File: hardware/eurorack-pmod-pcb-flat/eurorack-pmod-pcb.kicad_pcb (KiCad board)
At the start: 2 copper layers, 20 x 110 mm, 78 parts, among them J1 PMOD, J10 PJ398SM, J2 EURORACK_PWR, J3 PJ398SM, J4 PJ398SM, J5 PJ398SM, J6 PJ398SM, J7 PJ398SM, J8 PJ398SM, J9 PJ398SM, U1 LM1117-3.3, U2 TL072, U3 AK4619VN, U4 TL074, U5 TL074, U6 TL074, U7 TL074

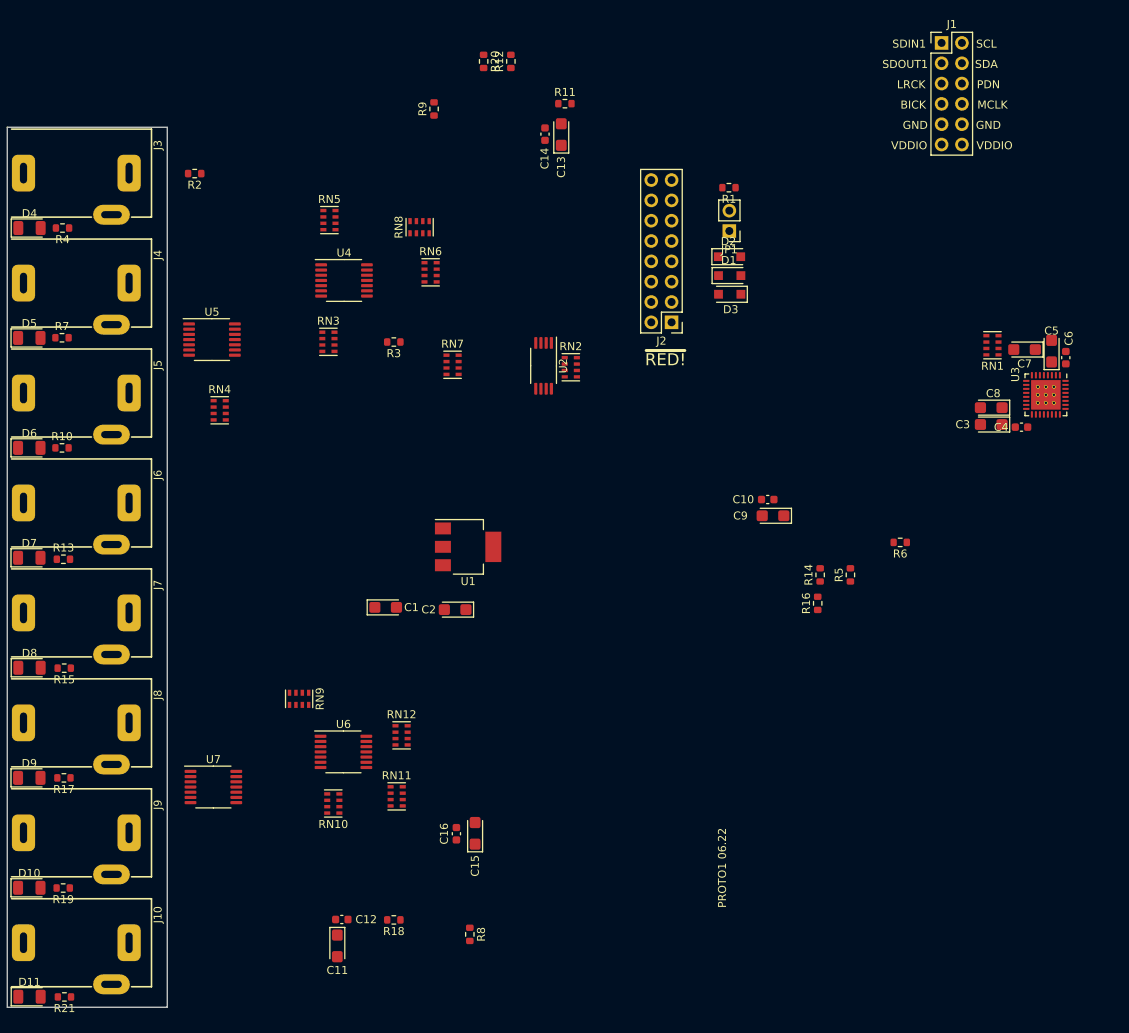
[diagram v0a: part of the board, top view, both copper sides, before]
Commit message: rev2-flat: add vref and stabilization caps
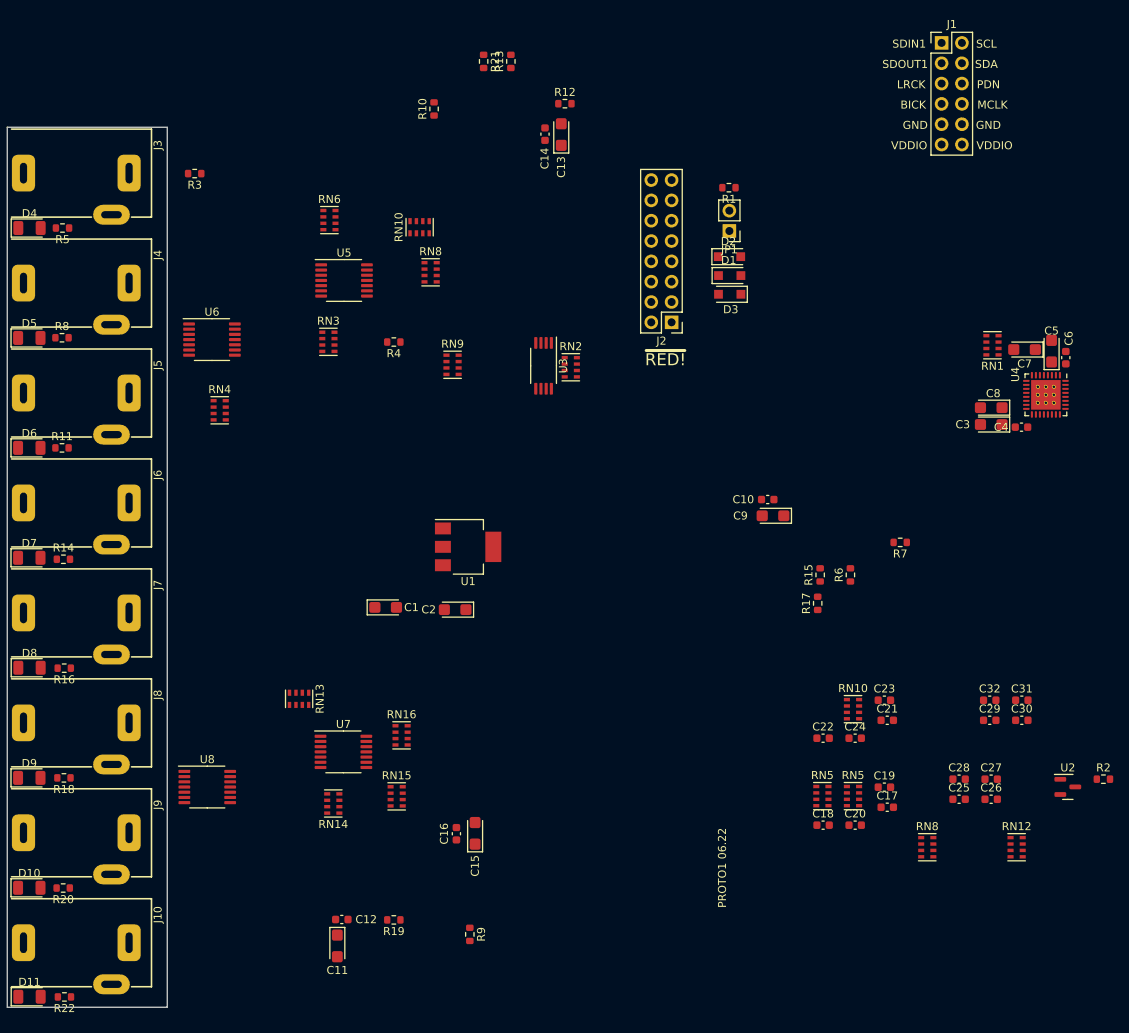
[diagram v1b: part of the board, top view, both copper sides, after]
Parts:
- added C17: 220p, Capacitor_SMD:C_0603_1608Metric, F.Cu at (90.0, 85.0)
- added C18: 220p, Capacitor_SMD:C_0603_1608Metric, F.Cu at (82.0, 87.2)
- added C19: 220p, Capacitor_SMD:C_0603_1608Metric, F.Cu at (89.6, 82.5)
- added C20: 220p, Capacitor_SMD:C_0603_1608Metric, F.Cu at (86.0, 87.2)
- added C21: 220p, Capacitor_SMD:C_0603_1608Metric, F.Cu at (90.0, 74.1)
- added C22: 220p, Capacitor_SMD:C_0603_1608Metric, F.Cu at (82.0, 76.4)
- added C23: 220p, Capacitor_SMD:C_0603_1608Metric, F.Cu at (89.6, 71.6)
- added C24: 220p, Capacitor_SMD:C_0603_1608Metric, F.Cu at (86.0, 76.4)
- added C25: 56p, Capacitor_SMD:C_0603_1608Metric, F.Cu at (99.0, 84.0)
- added C26: 220p, Capacitor_SMD:C_0603_1608Metric, F.Cu at (103.0, 84.0)
- added C27: 56p, Capacitor_SMD:C_0603_1608Metric, F.Cu at (103.0, 81.5)
- added C28: 220p, Capacitor_SMD:C_0603_1608Metric, F.Cu at (99.0, 81.5)
- added C29: 56p, Capacitor_SMD:C_0603_1608Metric, F.Cu at (102.8, 74.1)
- added C30: 220p, Capacitor_SMD:C_0603_1608Metric, F.Cu at (106.8, 74.1)
- added C31: 56p, Capacitor_SMD:C_0603_1608Metric, F.Cu at (106.8, 71.6)
- added C32: 220p, Capacitor_SMD:C_0603_1608Metric, F.Cu at (102.8, 71.6)
- added R2: 330R, Resistor_SMD:R_0603_1608Metric, F.Cu at (117.0, 81.5)
- added RN10: 15K, Resistor_SMD:R_Cat16-4, F.Cu at (85.7, 72.7)
- added RN12: 15K, Resistor_SMD:R_Cat16-4, F.Cu at (106.2, 90.0)
- added RN5: 15K, Resistor_SMD:R_Cat16-4, F.Cu at (85.7, 83.6)
- added RN5: 15K, Resistor_SMD:R_Cat16-4, F.Cu at (81.9, 83.6)
- added RN8: 15K, Resistor_SMD:R_Cat16-4, F.Cu at (95.0, 90.0)
- added U2: LM4040DBZ-3, Package_TO_SOT_SMD:SOT-23, F.Cu at (112.6, 82.5)
- moved U8 0.77 mm to (5.00, 82.5)
- renumbered R9 to R10, R10 to R11, R11 to R12, R12 to R13, R13 to R14, R14 to R15, R15 to R16, R16 to R17, R17 to R18, R18 to R19, R19 to R20, R20 to R21, R21 to R22, R2 to R3, R3 to R4, R4 to R5, R5 to R6, R6 to R7, R7 to R8, R8 to R9, RN8 to RN10, RN9 to RN13, RN10 to RN14, RN11 to RN15, RN12 to RN16, RN5 to RN6, RN6 to RN8, RN7 to RN9, U2 to U3, U3 to U4, U4 to U5, U5 to U6, U6 to U7, U7 to U8
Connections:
- J10 pad TN: GND -> unconnected-(J10-PadTN)
- J7 pad TN: GND -> unconnected-(J7-PadTN)
- J8 pad TN: GND -> unconnected-(J8-PadTN)
- J9 pad TN: GND -> unconnected-(J9-PadTN)
- RN2 pad 8: +3.3VA -> /VREFH
- U4 pad 21: +3.3VA -> /VREFH
- U6 pad 13: Net-(D7-Pad1) -> Net-(C24-Pad1)
- U6 pad 2: Net-(D4-Pad1) -> Net-(C18-Pad1)
- U6 pad 6: Net-(D5-Pad1) -> Net-(C20-Pad1)
- U6 pad 9: Net-(D6-Pad1) -> Net-(C22-Pad1)
- U8 pad 13: Net-(D11-Pad2) -> Net-(C32-Pad1)
- U8 pad 2: Net-(D8-Pad2) -> Net-(C26-Pad1)
- U8 pad 6: Net-(D9-Pad2) -> Net-(C28-Pad1)
- U8 pad 9: Net-(D10-Pad2) -> Net-(C30-Pad1)

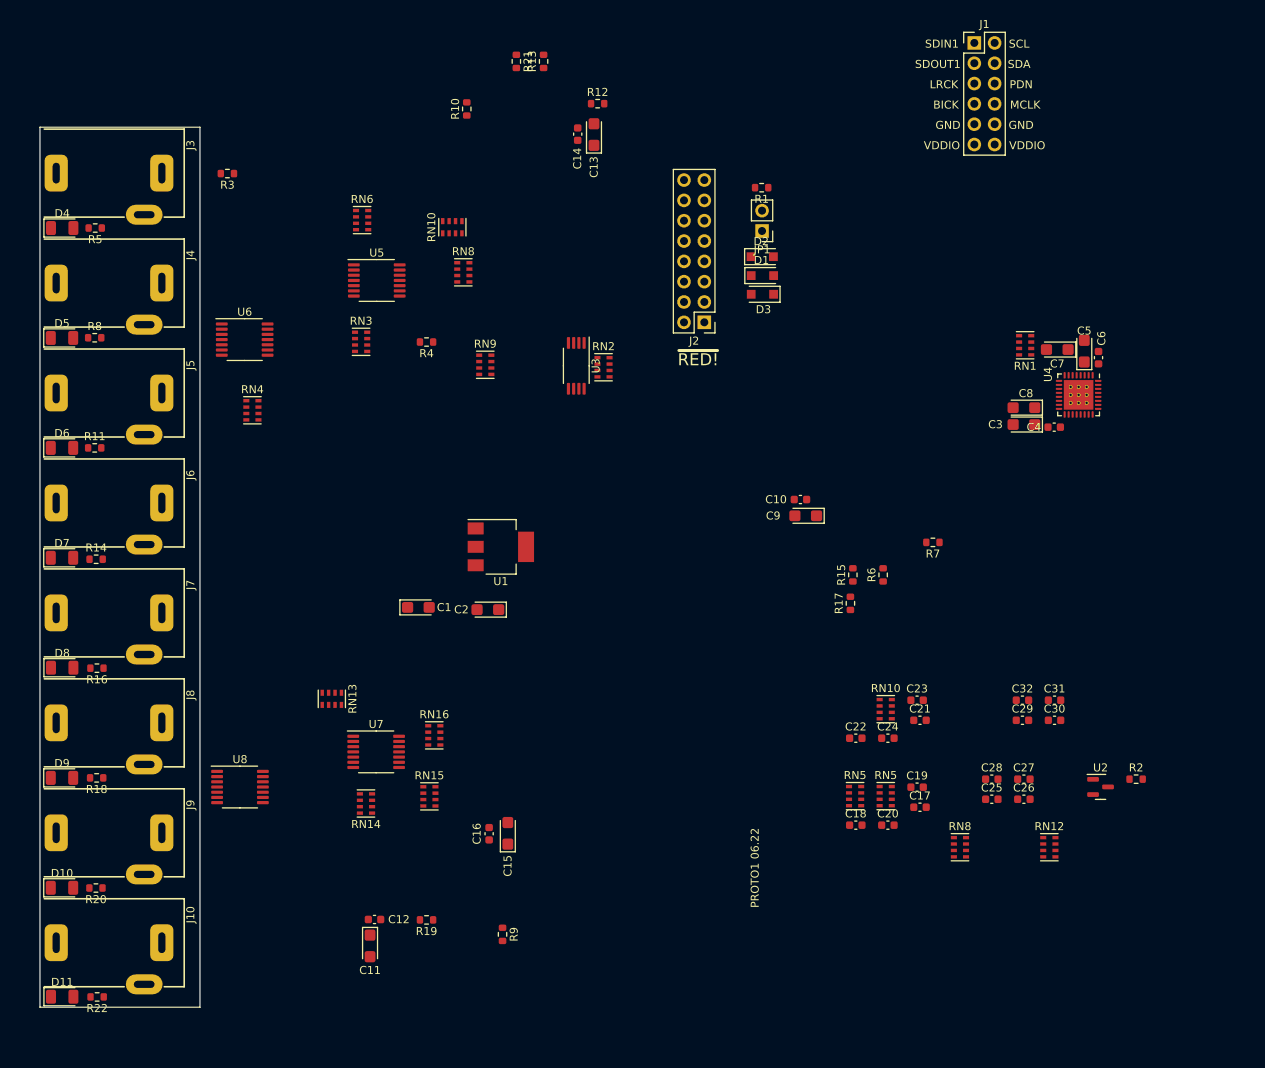
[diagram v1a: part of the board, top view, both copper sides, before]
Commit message: rev2-flat: update power supply and add bypass electros
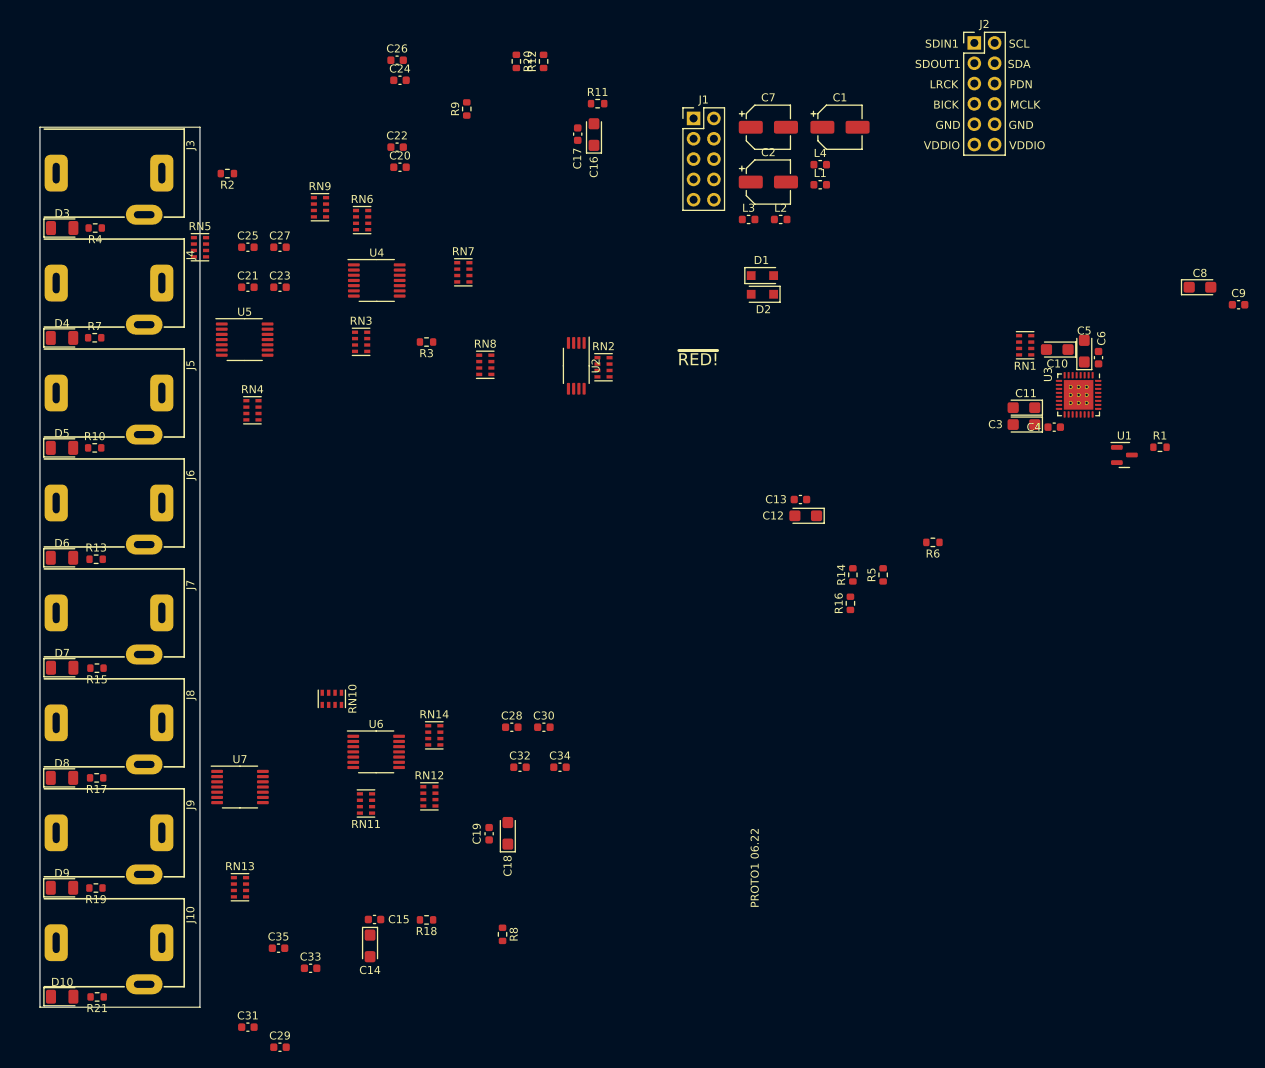
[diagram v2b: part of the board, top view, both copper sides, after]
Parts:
- removed the D2 at (70.3, 16.2)
- removed the J2 at (63.0, 24.4)
- removed JP1: JUMPER_3V3, Connector_PinHeader_2.54mm:PinHeader_1x02_P2.54mm_Vertical
- removed the R1 at (70.2, 7.55)
- removed the RN10 at (31.5, 12.5)
- removed the RN5 at (85.7, 83.6)
- removed the RN8 at (95.0, 90.0)
- removed the U1 at (37.6, 52.5)
- added C7: 47u, Capacitor_SMD:CP_Elec_5x5.3, F.Cu at (71.0, 0.00)
- added C8: 10u, Capacitor_Tantalum_SMD:CP_EIA-3216-10_Kemet-I, F.Cu at (125.0, 20.0)
- added C9: 100n, Capacitor_SMD:C_0603_1608Metric, F.Cu at (129.8, 22.2)
- added J1: EURORACK_PWR, Connector_PinHeader_2.54mm:PinHeader_2x05_P2.54mm_Vertical, F.Cu at (61.7, -1.10)
- added L1: Ferrite, Inductor_SMD:L_0603_1608Metric, F.Cu at (77.5, 7.19)
- added L2: Ferrite, Inductor_SMD:L_0603_1608Metric, F.Cu at (72.6, 11.5)
- added L3: Ferrite, Inductor_SMD:L_0603_1608Metric, F.Cu at (68.6, 11.5)
- added L4: Ferrite, Inductor_SMD:L_0603_1608Metric, F.Cu at (77.5, 4.68)
- C1, C2: value 10u -> 47u; footprint Capacitor_Tantalum_SMD:CP_EIA-3216-10_Kemet-I -> Capacitor_SMD:CP_Elec_5x5.3
- moved RN5 106.8 mm to (0.00, 15.0)
- moved C20 103.1 mm to (25.0, 5.00)
- moved C22 103.1 mm to (24.6, 2.49)
- moved C24 103.1 mm to (25.0, -5.87)
- moved C26 103.1 mm to (24.6, -8.38)
- moved C21 101.5 mm to (5.99, 20.0)
- moved C23 101.5 mm to (10.0, 20.0)
- moved RN13 101.3 mm to (5.00, 95.0)
- moved C31 98.0 mm to (5.99, 112.5)
- moved C35 98.0 mm to (9.82, 102.6)
- moved C29 98.0 mm to (10.0, 115.0)
- moved C33 98.0 mm to (13.8, 105.1)
- moved C25 97.7 mm to (5.99, 15.0)
- moved C27 97.7 mm to (10.0, 15.0)
- moved RN9 94.5 mm to (15.0, 10.0)
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- renumbered C7 to C10, C8 to C11, C9 to C12, C10 to C13, C11 to C14, C12 to C15, C13 to C16, C14 to C17, C15 to C18, C16 to C19, C17 to C20, C18 to C21, C19 to C22, C20 to C23, C21 to C24, C22 to C25, C23 to C26, C24 to C27, C25 to C28, C26 to C29, C27 to C30, C28 to C31, C29 to C32, C30 to C33, C31 to C34, C32 to C35, D11 to D10, D3 to D2, D4 to D3, D5 to D4, D6 to D5, D7 to D6, D8 to D7, D9 to D8, D10 to D9, J1 to J2, R2 to R1, R11 to R10, R12 to R11, R13 to R12, R14 to R13, R15 to R14, R16 to R15, R17 to R16, R18 to R17, R19 to R18, R20 to R19, R3 to R2, R21 to R20, R22 to R21, R4 to R3, R5 to R4, R6 to R5, R7 to R6, R8 to R7, R9 to R8, R10 to R9, RN13 to RN10, RN14 to RN11, RN15 to RN12, RN12 to RN13, RN16 to RN14, RN8 to RN7, RN9 to RN8, RN10 to RN9, U2 to U1, U3 to U2, U4 to U3, U5 to U4, U6 to U5, U7 to U6, U8 to U7
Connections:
- C1 pad 1: +5V -> +12V
- C2 pad 1: +3.3VA -> GND
- C2 pad 2: GND -> -12V
- D1 pad 1: +12V -> Net-(D1-Pad1)
- D1 pad 2: GND -> Net-(D1-Pad2)
- D2 pad 1: GND -> Net-(D2-Pad1)
- D2 pad 2: -12V -> Net-(D2-Pad2)

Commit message: rev2-flat: layout most components
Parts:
- moved C1 119.2 mm to (5.08, 92.7), turned to 90 degrees
- moved C2 119.1 mm to (5.08, 106.0), turned to 90 degrees
- moved R20 117.3 mm to (0.19, 102.2), turned to 180 degrees
- moved L1 115.1 mm to (6.50, 97.8)
- moved C9 114.3 mm to (17.1, 41.3)
- moved J1 114.3 mm to (17.1, 104.1), turned to 180 degrees
- moved C8 113.6 mm to (14.0, 44.1), turned to -90 degrees
- moved C6 113.3 mm to (3.17, 59.3), turned to -90 degrees
- moved L2 111.3 mm to (6.34, 101.0)
- moved C5 109.8 mm to (5.51, 60.1), turned to -90 degrees
- moved U3 106.9 mm to (4.92, 53.8), turned to 90 degrees
- moved J2 106.5 mm to (14.6, 57.1)
- moved C10 102.9 mm to (9.53, 60.3), turned to 0 degrees
- moved R1 102.6 mm to (17.8, 48.9), turned to -90 degrees
- moved D2 101.7 mm to (10.2, 102.9), turned to 90 degrees
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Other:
- board size 20 x 110 mm -> 42 x 110 mm
- board text added: "+12"
- board text added: "-12"
- board text added: "3V3"
- board text added: "PMOD"
- board text added: "PROTO2 30.07.22"
- board text removed: "BICK"
- board text removed: "LRCK"
- board text removed: "MCLK"
- board text removed: "PDN"
- board text removed: "PROTO1 06.22"
- board text removed: "SCL"
- board text removed: "SDA"
- board text removed: "SDIN1"
- board text removed: "SDOUT1"
- board text removed: "VDDIO"

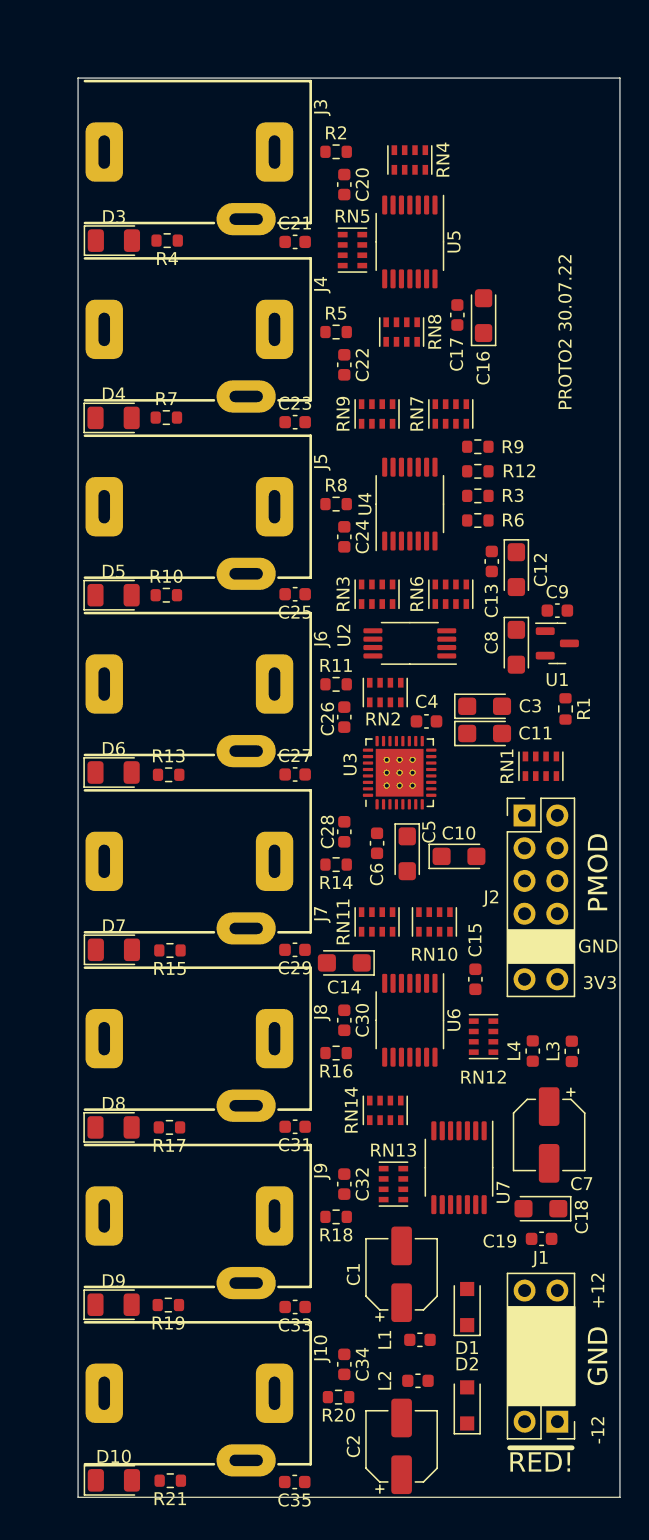
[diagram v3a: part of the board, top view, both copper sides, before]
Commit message: rev2-flat: finish component layout
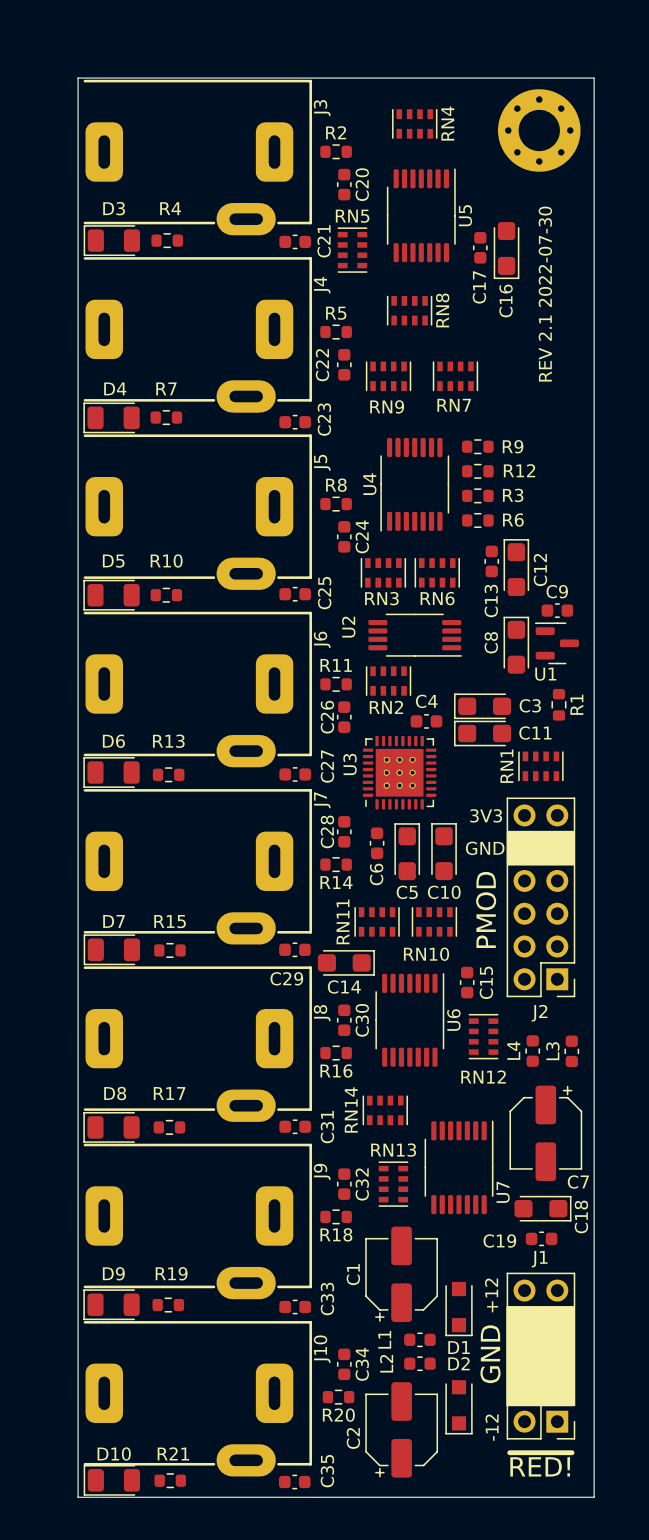
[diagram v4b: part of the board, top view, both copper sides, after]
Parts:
- added REF**: MountingHole_3.2mm_M3_Pad_Via, MountingHole:MountingHole_3.2mm_M3_Pad_Via, F.Cu at (15.7, 4.06)
- moved J2 13.0 mm to (17.1, 69.8), turned to 180 degrees
- moved C17 5.50 mm to (11.2, 13.2)
- moved C16 5.50 mm to (13.2, 13.2)
- moved RN9 3.06 mm to (4.06, 23.1)
- moved RN7 2.95 mm to (9.25, 23.1)
- moved RN4 2.82 mm to (6.10, 3.56)
- moved U5 2.22 mm to (6.60, 10.7)
- moved RN6 1.96 mm to (7.84, 38.3)
- moved RN8 1.76 mm to (5.70, 18.0)
- moved RN3 1.72 mm to (3.66, 38.4)
- moved U4 1.57 mm to (6.10, 31.5)
- moved L2 1.33 mm to (6.50, 99.6)
- moved C2 1.28 mm to (5.08, 104.8)
- moved C10 1.18 mm to (8.37, 60.1), turned to -90 degrees
- moved RN2 0.92 mm to (4.06, 46.7)
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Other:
- board size 42 x 110 mm -> 40 x 110 mm
- board text added: "REV 2.1 2022-07-30"
- board text removed: "PROTO2 30.07.22"
